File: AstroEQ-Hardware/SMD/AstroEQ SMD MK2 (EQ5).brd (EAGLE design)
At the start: 85 x 49 mm, 41 parts, among them IC1 ATMEGA162-16AU, IC2 PIC18F14K50-I/SS, IC3 78L05, J1 POWER_JACKPANEL, M1 Motor Driver, M2 Motor Driver, SW1 SWITCH, X1 16MHz, X2 12MHz

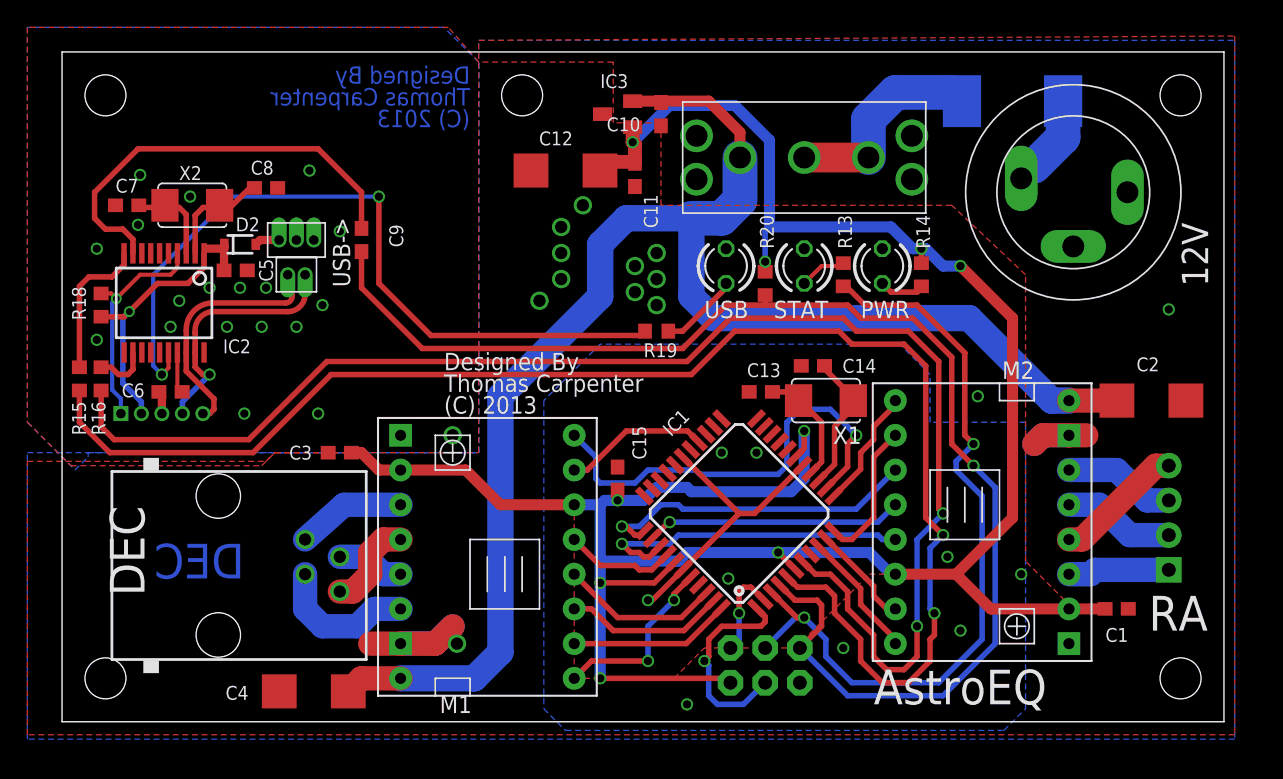
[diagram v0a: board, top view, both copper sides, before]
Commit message: Added SMD design to fit inside EQ5 mount shell.
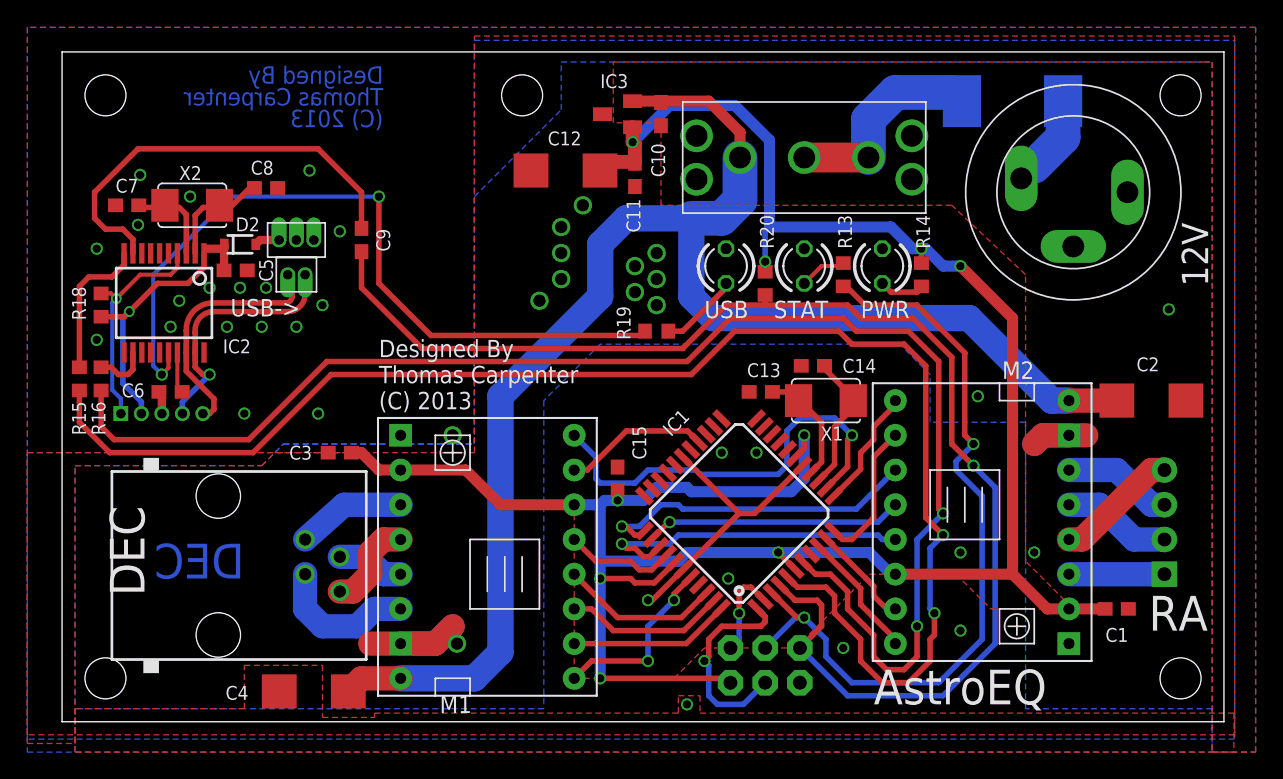
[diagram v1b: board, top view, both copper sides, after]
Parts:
- USB->: value Bulgin PX0458 -> Bulgin PX0447
- moved JP1 0.45 mm to (80.6, 10.8)
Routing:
- net +5V: track 180.8 -> 178.6 mm
- net DIR-1: track 33.0 -> 31.6 mm
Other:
- board text added: "I use iteadstudio.com 10cm x 5cm prototype service, selecting 1.2mm thick, HASL, 100% electrical check"
- board text added: "It is a 2 Layer board designed to be sent for manufacture. The AstroEQ-SMD-Gerber.zip file contains the required gerber files."
- board text added: "The board uses some very tricky surface mount components and is not recommended for DIY."
- board text added: "This board design is for AstroEQ boards which fit inside the enclosure on an EQ5 Mount."
- board text removed: "4988"
- board text removed: "8824/5"
- board text removed: "Markings show the location of the Potentiometers on the"
- board text removed: "Pololu Boards depending on which chip they use."
- board text removed: "Sq Pad"
